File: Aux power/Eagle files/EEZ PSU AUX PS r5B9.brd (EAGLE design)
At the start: 100 x 74 mm, 85 parts, among them IC16 LM25575MH/NOPB, IC17 TPD4E002DRLR, IC18 TPD2E001DZDR, IC19 ADUM3160BRWZ, Q20 BTA26-600, Q21 BTA26-600, Q22 IRLL014N, X10 826629-5, X11 2411-01, X4 39303055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

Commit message: AUX PS: R107 value changed
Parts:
- R107: value 15R/7W -> 22R/7W
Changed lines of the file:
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@@
 <attribute name="VALUE" x="17.0815" y="10.9855" size="1.27" layer="27" ratio="10" rot="R270"/>
 </element>
-<element name="R107" library="EEZ_Lib1" package="R_0913" value="15R/7W" x="34.671" y="10.541" smashed="yes" rot="R270">
+<element name="R107" library="EEZ_Lib1" package="R_0913" value="22R/7W" x="34.671" y="10.541" smashed="yes" rot="R270">
 <attribute name="NAME" x="31.8135" y="1.8034" size="1.6764" layer="25" ratio="10"/>
 <attribute name="VALUE" x="31.115" y="10.9093" size="1.27" layer="27" ratio="10"/>

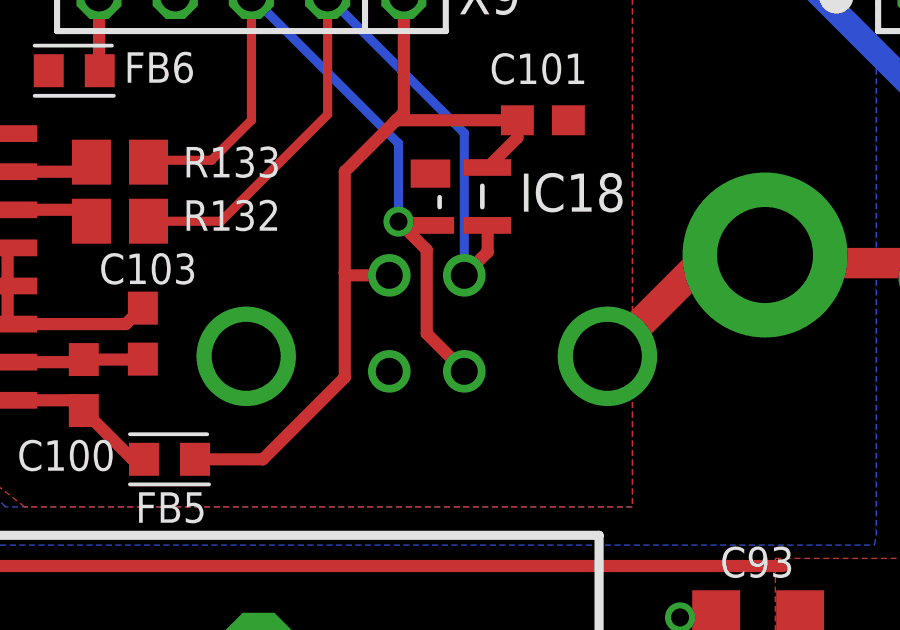
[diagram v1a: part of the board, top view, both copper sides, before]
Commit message: Small corrections on top silkscreen
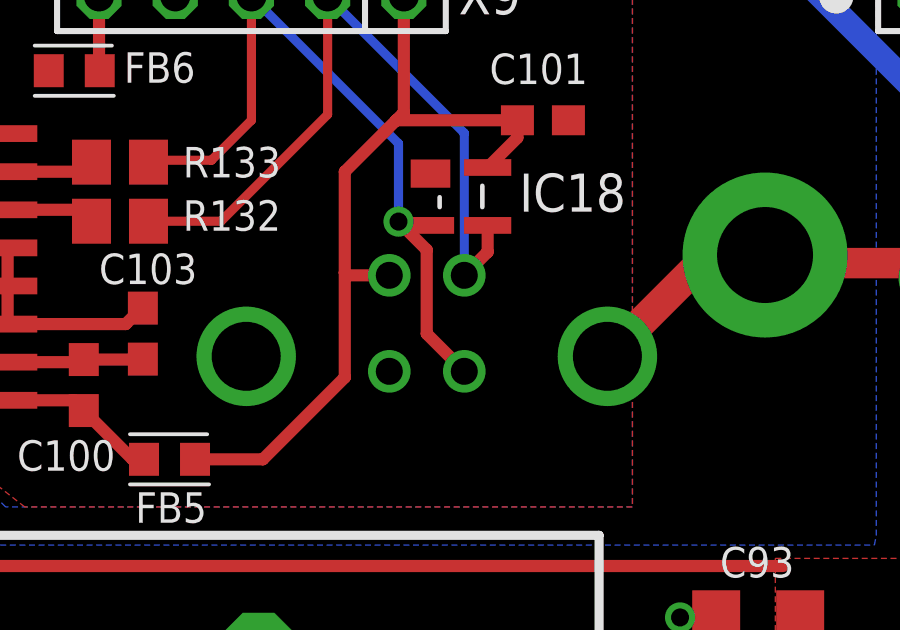
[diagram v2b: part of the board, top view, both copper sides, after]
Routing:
- net D+: vias 2 -> 1
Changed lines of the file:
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@@
 <layer number="27" name="tValues" color="10" fill="1" visible="no" active="yes"/>
 <layer number="28" name="bValues" color="11" fill="1" visible="no" active="yes"/>
-<layer number="29" name="tStop" color="7" fill="3" visible="yes" active="yes"/>
+<layer number="29" name="tStop" color="7" fill="3" visible="no" active="yes"/>
 <layer number="30" name="bStop" color="7" fill="6" visible="no" active="yes"/>
 <layer number="31" name="tCream" color="7" fill="4" visible="no" active="yes"/>
@@
 <layer number="37" name="tTest" color="7" fill="1" visible="no" active="yes"/>
 <layer number="38" name="bTest" color="7" fill="1" visible="no" active="yes"/>
-<layer number="39" name="tKeepout" color="15" fill="1" visible="yes" active="yes"/>
+<layer number="39" name="tKeepout" color="15" fill="1" visible="no" active="yes"/>
 <layer number="40" name="bKeepout" color="13" fill="1" visible="no" active="yes"/>
 <layer number="41" name="tRestrict" color="4" fill="10" visible="no" active="yes"/>
@@
 <wire x1="61.849" y1="63.4873" x2="60.9092" y2="63.4873" width="0.4064" layer="1"/>
 <wire x1="60.9092" y1="63.4873" x2="60.7822" y2="63.6143" width="0.4064" layer="1"/>
-<wire x1="62.9755" y1="58.623" x2="62.9755" y2="58.627" width="0.4064" layer="16"/>
-<wire x1="62.9755" y1="58.627" x2="61.722" y2="59.8805" width="0.4064" layer="1"/>
-<wire x1="61.722" y1="59.8805" x2="61.722" y2="62.6745" width="0.4064" layer="1"/>
+<wire x1="62.9755" y1="58.623" x2="62.9755" y2="58.627" width="0" layer="19" extent="1-16"/>
+<wire x1="61.722" y1="59.8765" x2="61.722" y2="62.6745" width="0.4064" layer="1"/>
 <wire x1="61.722" y1="62.6745" x2="60.7822" y2="63.6143" width="0.4064" layer="1"/>
-<via x="62.9755" y="58.627" extent="1-16" drill="0.6" shape="octagon"/>
+<wire x1="61.722" y1="59.8765" x2="62.9755" y2="58.623" width="0.4064" layer="1"/>
 </signal>
 <signal name="XUSB_VBUS">
@@
 </signal>
 </signals>
+<errors>
+</errors>
 </board>
 </drawing>
